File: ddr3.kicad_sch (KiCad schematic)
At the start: 19 parts, among them U8 MT41K128M16JT-125_K

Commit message: Added loclib
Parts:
- C33, C34, C35, C36, C37, C38, C39, C40, C41, C42: footprint antmicro-footprints:0402-cap -> crosslink-nx-video-converter-footprints:0402-cap; symbol antmicroCapacitors0402:C_100n_0402 -> crosslink-nx-video-converter:C_100n_0402
- R47: footprint antmicro-footprints:0402-res -> crosslink-nx-video-converter-footprints:0402-res; symbol antmicroResistors0402:R_100R_0402 -> crosslink-nx-video-converter:R_100R_0402
- R48, R49, R50, R51, R52, R53: footprint antmicro-footprints:R_Array_4x0402 -> crosslink-nx-video-converter-footprints:R_Array_4x0402; symbol antmicroResistorNetworksArrays:4x51R_0402_array -> crosslink-nx-video-converter:4x51R_0402_array
- R54: footprint antmicro-footprints:0402-res -> crosslink-nx-video-converter-footprints:0402-res; symbol antmicroResistors0402:R_240R_1%_0402 -> crosslink-nx-video-converter:R_240R_1%_0402
- U8: footprint antmicro-footprints:BGA80P96C6X16_800X1400X110 -> crosslink-nx-video-converter-footprints:BGA80P96C6X16_800X1400X110; symbol antmicroMemory:MT41K128M16JT-125_K -> crosslink-nx-video-converter:MT41K128M16JT-125_K

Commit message: Divided FPGA into multiple blocks
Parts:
- added C? (x6): C_100n_0603, crosslink-nx-video-converter-footprints:0603-cap, symbol crosslink-nx-video-converter:C_100n_0603
- added U? (x2): LIFCL-40-9BG256C, antmicro-footprints:BGA-256_16x16_14.0x14.0mm, symbol antmicroBGAchips:LIFCL-40-9BG256C
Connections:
- net +1V35: now also C?.1, C?.1, C?.1, C?.1, U?.N6 (VCCIO4), U?.P11 (PB54B/PCLKC3_0/ADC_CN5 ), U?.P12 (VCCIO3), U?.R2 (PB16B)
- net DDR3_A0: now also U?.N13 (PB70B/COMP2IN )
- net DDR3_A1: now also U?.P15 (PB72A/PCLKT3_2/ADC_CP13)
- net DDR3_A10: now also U?.L12 (PB82B/ADC_CN15)
- net DDR3_A11: now also U?.M16 (PB84A/LRC_GPLL0T_IN)
- net DDR3_A12: now also U?.T7 (PB30A)
- net DDR3_A13: now also U?.T8 (PB30B)
- net DDR3_A2: now also U?.P16 (PB72B/PCLKC3_2/ADC_CN13)
- net DDR3_A3: now also U?.M14 (PB74A/PCLKT3_3/ADC_CP14)
- net DDR3_A4: now also U?.N16 (PB76A/COMP3IP)
- net DDR3_A5: now also U?.N15 (PB76B/COMP3IN)
- net DDR3_A6: now also U?.M12 (PB78A/ADC_CP11)
- net DDR3_A7: now also U?.L11 (PB80A/ADC_CP12)
- net DDR3_A8: now also U?.L10 (PB80B/ADC_CN12)
- net DDR3_A9: now also U?.M13 (PB82A/ADC_CP15)
- net DDR3_BA0: now also U?.P6 (PB32A)
- net DDR3_BA1: now also U?.P7 (PB32B)
- net DDR3_BA2: now also U?.L8 (PB34A)
- net DDR3_CKE: now also U?.P9 (PB44B/PCLKC4_0)
- net DDR3_CK_N: now also U?.T10 (PB40B/PCLKC4_1)
- net DDR3_CK_P: now also U?.T9 (PB40A/PCLKT4_1)
- net DDR3_DQ0: now also U?.R3 (PB18A/PCLKT4_3 )
- net DDR3_DQ1: now also U?.T3 (PB20A)
- net DDR3_DQ10: now also U?.T11 (PB58B/PCLKC3_1/ADC_CN6 )
- net DDR3_DQ11: now also U?.R13 (PB62A/ADC_CP10)
- net DDR3_DQ12: now also U?.R14 (PB62B/ADC_CN10)
- net DDR3_DQ13: now also U?.T14 (PB66A/COMP1IP)
- net DDR3_DQ14: now also U?.T15 (PB66B/COMP1IN)
- net DDR3_DQ15: now also U?.R16 (PB68A/ADC_CP8)
- net DDR3_DQ2: now also U?.T4 (PB20B)
- net DDR3_DQ3: now also U?.R4 (PB24A/PCLKT4_2)
- net DDR3_DQ4: now also U?.T5 (PB26A)
- net DDR3_DQ5: now also U?.R6 (PB26B)
- net DDR3_DQ6: now also U?.T6 (PB28A)
- net DDR3_DQ7: now also U?.R7 (PB28B)
- net DDR3_DQ8: now also U?.R10 (PB56B/ADC_CN7 )
- net DDR3_DQ9: now also U?.T12 (PB58A/PCLKT3_1/ADC_CP6 )
- net DDR3_LDM: now also U?.T2 (PB18B/PCLKC4_3 )
- net DDR3_LDQS_N: now also U?.P5 (PB22B)
- net DDR3_LDQS_P: now also U?.R5 (PB22A)
- net DDR3_ODT: now also U?.M10 (PB46A)
- net DDR3_UDM: now also U?.R15 (PB68B/ADC_CN8)
- net DDR3_UDQS_N: now also U?.T13 (PB60B/ADC_CN9)
- net DDR3_UDQS_P: now also U?.R12 (PB60A/ADC_CP9)
- net GND: now also C?.2, C?.2, C?.2, C?.2, U?.M11 (PB78B/ADC_CN11), U?.M15 (PB84B/LRC_GPLL0C_IN/VREF3_2), U?.M8 (PB38B), U?.M9 (PB38A), U?.N11 (PB64B/ADC_CN4), U?.N12 (PB64A/ADC_CP4), U?.N14 (PB74B/PCLKC3_3/ADC_CN14), U?.P10 (PB56A/ADC_CP7 ), U?.P14 (PB70A/COMP2IP), U?.P4 (PB24B/PCLKC4_2 ), U?.R8 (PB42A), U?.R9 (PB44A/PCLKT4_0)
- net Vref: now also C?.1, C?.1, C?.2, C?.2, U?.R1 (PB16A/VREF4_1), U?.R11 (PB54A/PCLKT3_0/VREF3_1/ADC_CP5)
- net ~{DDR3_CAS}: now also U?.N8 (PB36A)
- net ~{DDR3_CS}: now also U?.P8 (PB42B)
- net ~{DDR3_RAS}: now also U?.L9 (PB34B)
- net ~{DDR3_RESET}: now also U?.N10 (PB46B/VREF4_2)
- net ~{DDR3_WE}: now also U?.N9 (PB36B)
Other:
- note added: "FPGA"
- note added: "RAM"
- note added: "TERMINATION"
- note removed: "MT41K128M16JT"
- moved on the sheet: C33, C34, C35, C36, C37, C38, C39, C40, C41, C42, R47, R48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

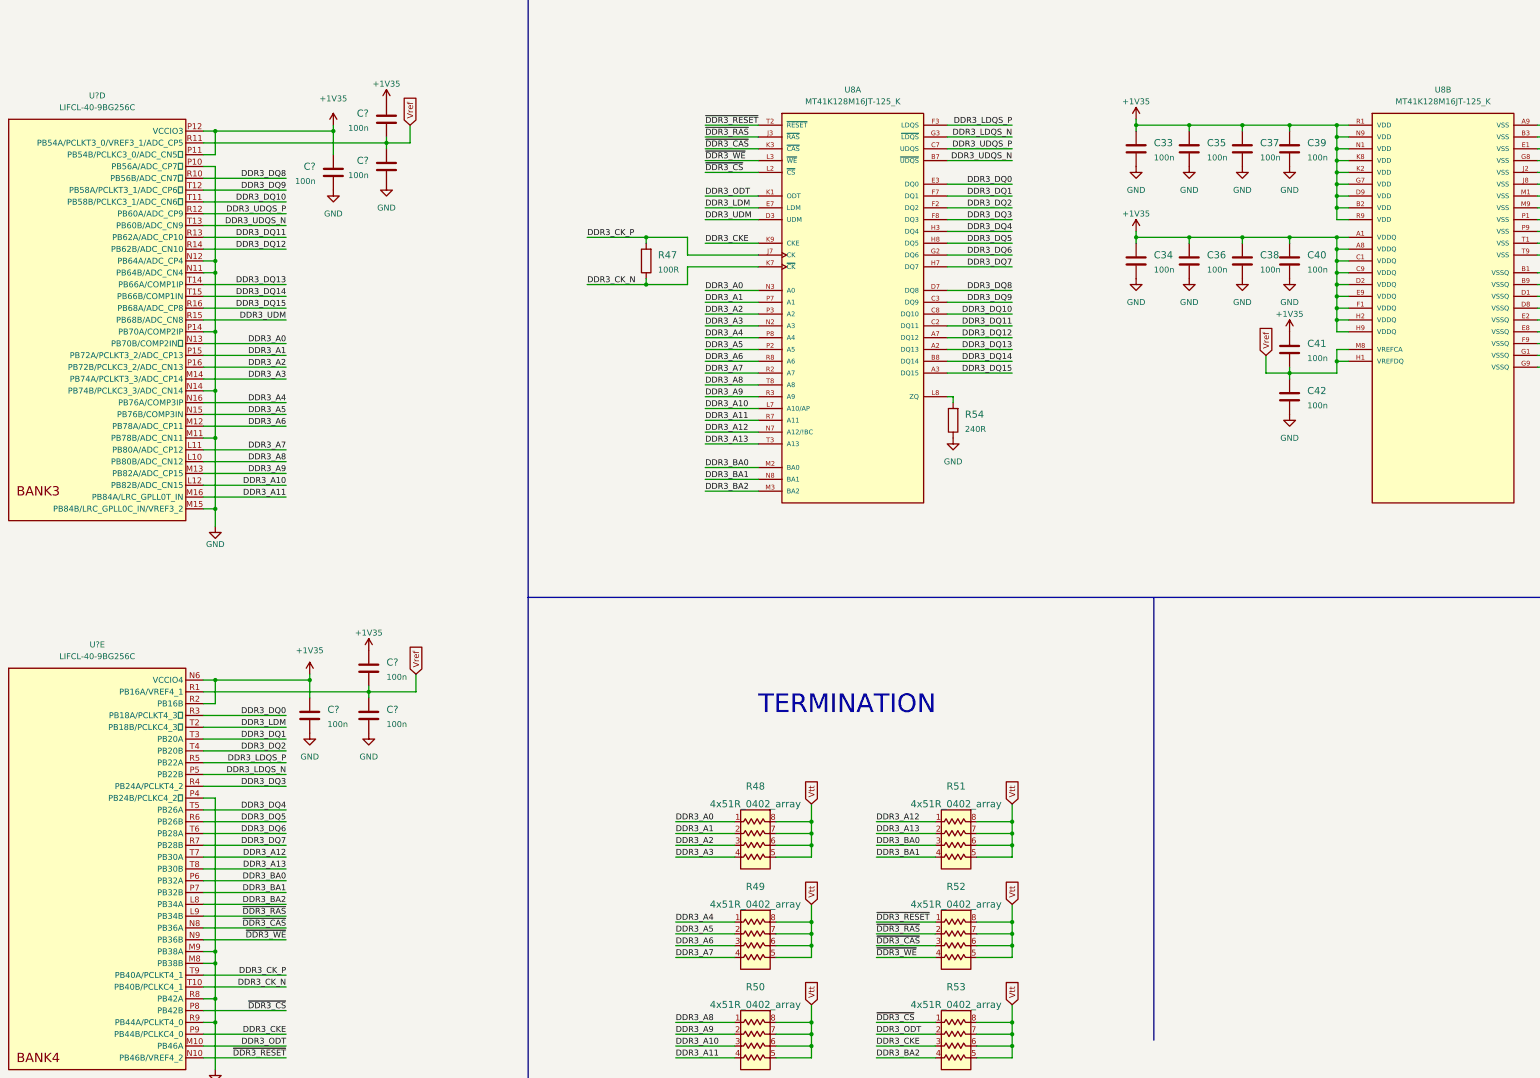
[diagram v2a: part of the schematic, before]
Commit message: Modified power indicator and connected unused pins
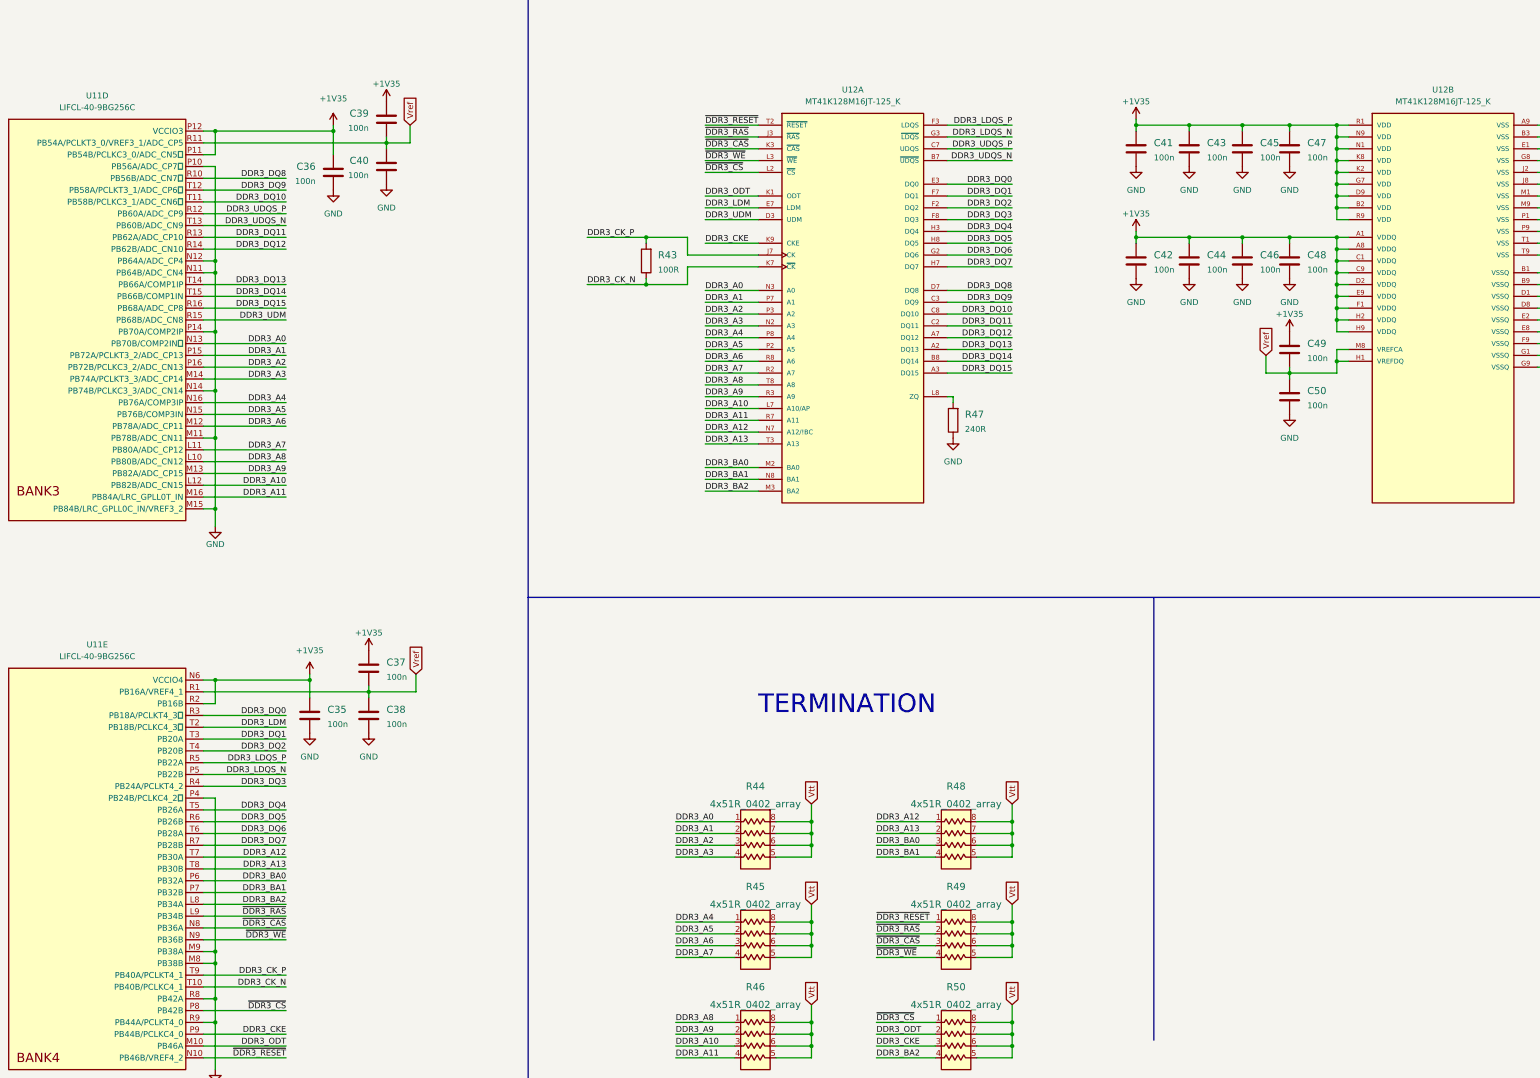
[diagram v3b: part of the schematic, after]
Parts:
- gave numbers to parts that had none: 7
- renumbered C33 to C41, C34 to C42, C35 to C43, C36 to C44, C37 to C45, C38 to C46, C39 to C47, C40 to C48, C41 to C49, C42 to C50, R47 to R43, R48 to R44, R49 to R45, R50 to R46, R54 to R47, R51 to R48, R52 to R49, R53 to R50, U8 to U12
